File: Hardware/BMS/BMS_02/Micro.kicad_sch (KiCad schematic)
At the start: 21 parts, among them U1 PIC33EP256MC506, U17 CD4051B, U26 CD4051B, U5 CD4051B, Y1 8MHz

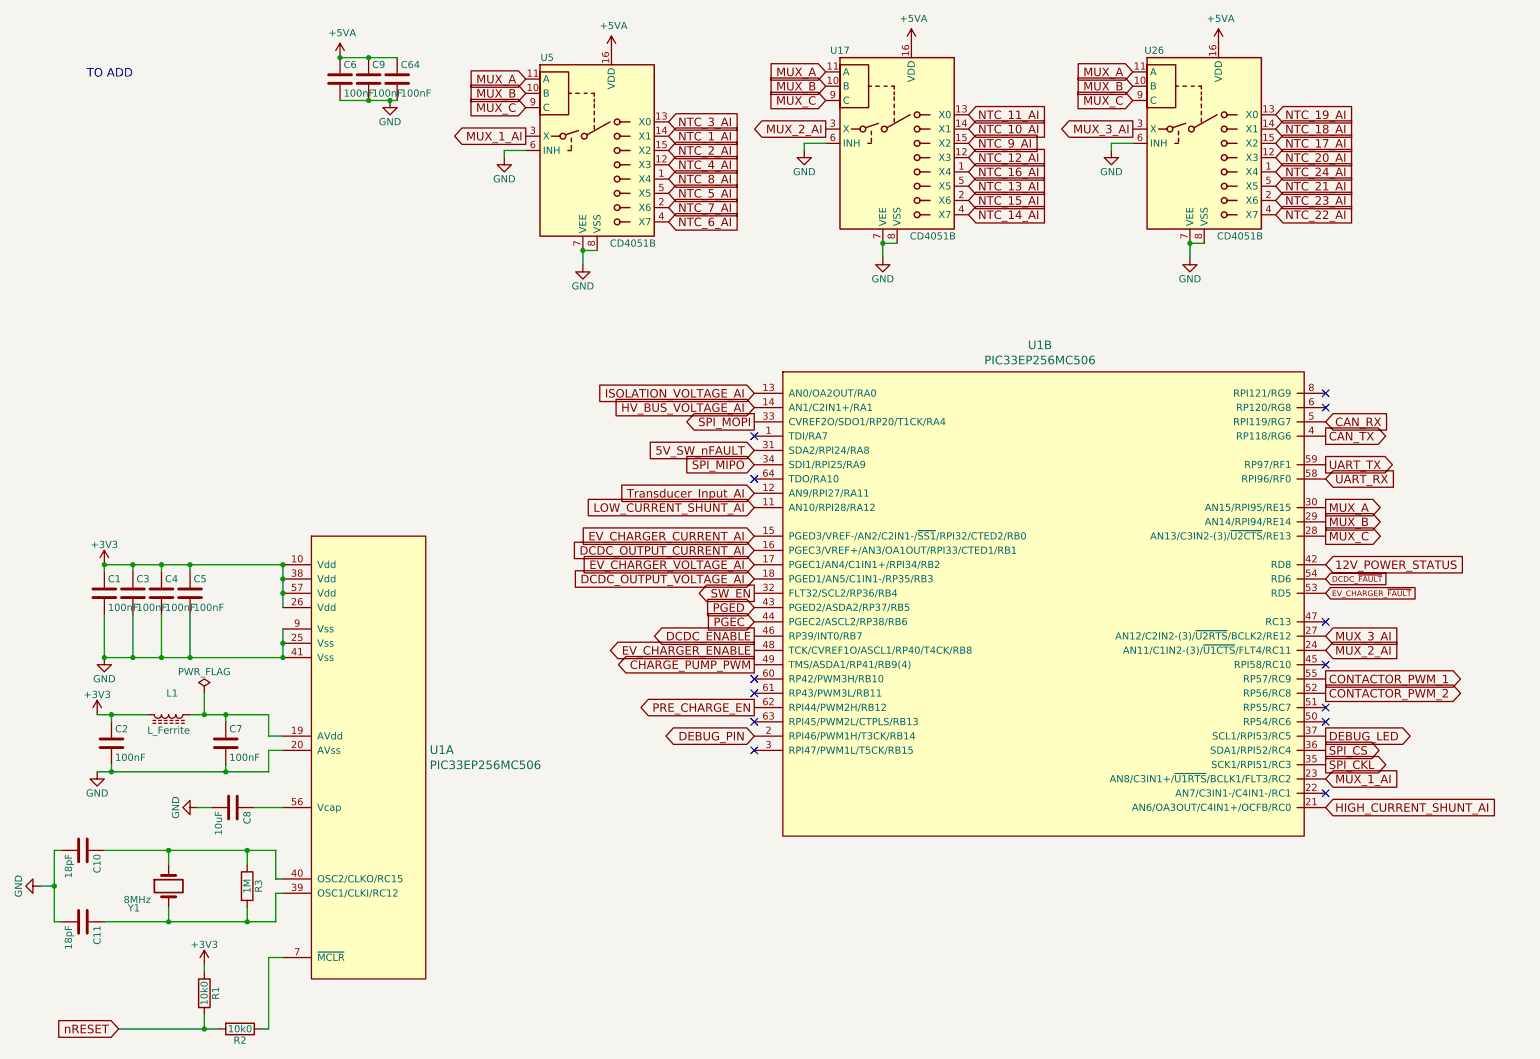
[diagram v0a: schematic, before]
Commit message: bms 02 build and code bring up. Board is built, bootloader is stable and uploads app flawlessly.
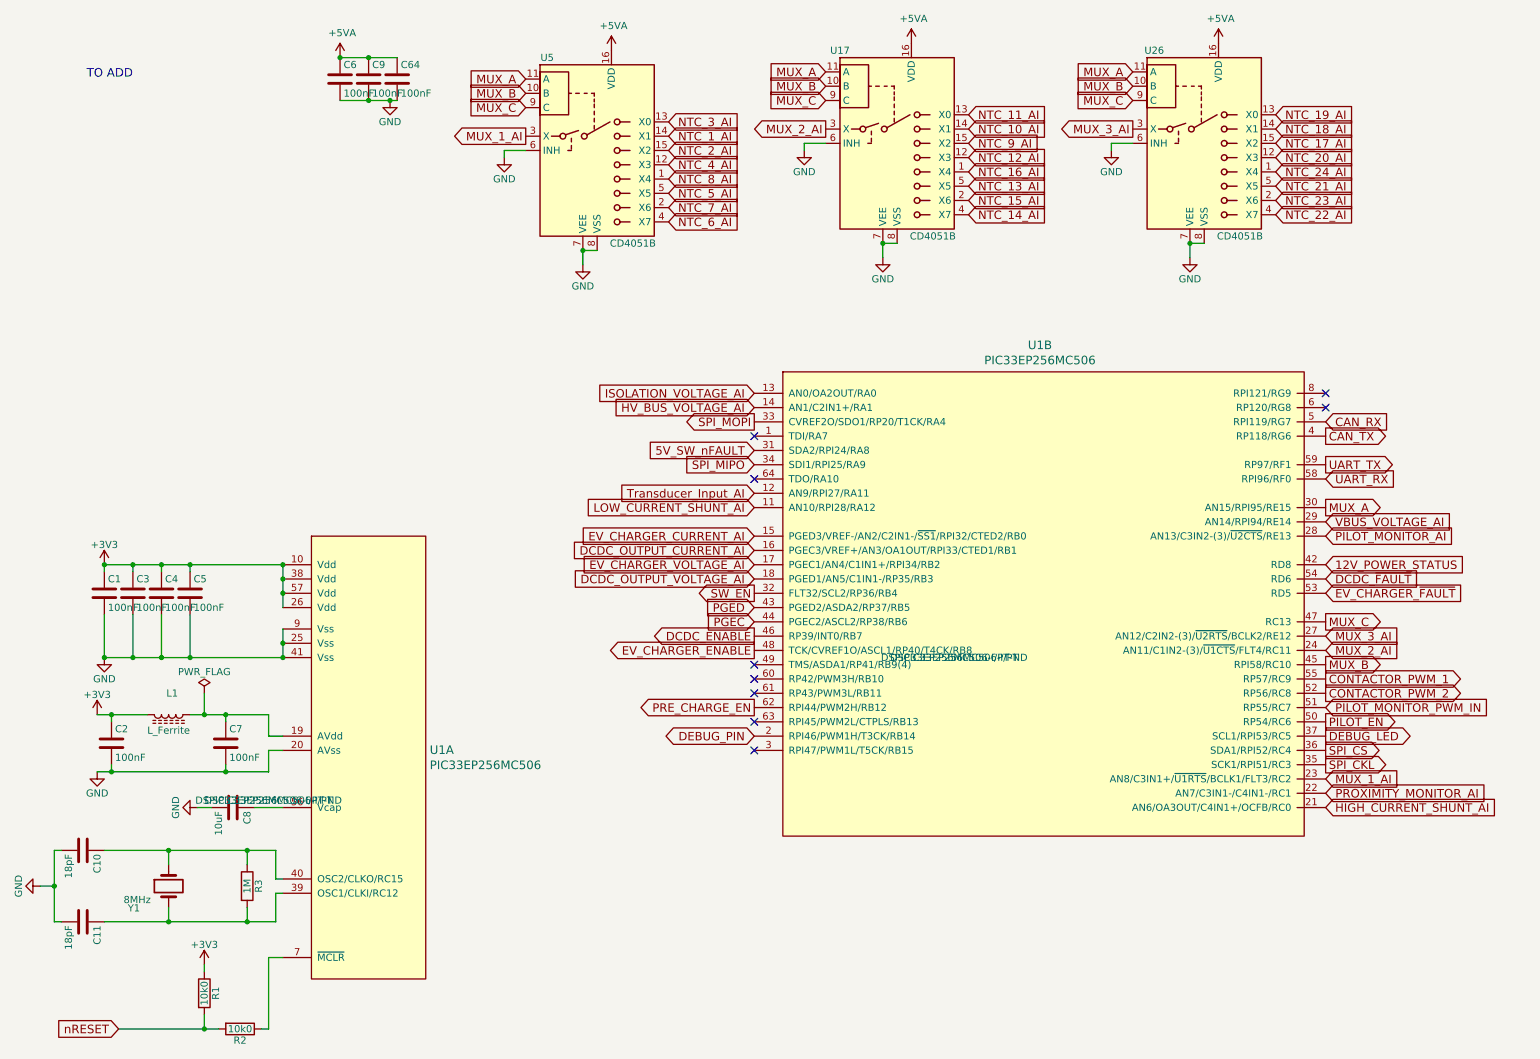
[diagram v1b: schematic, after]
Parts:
- C1, C10, C11, C2, C3, C4, C5, C6, C64, C7, C8, C9, L1, R1, R2, R3: DNP (none) -> (none)
- U1: Digikey_PN (none) -> DSPIC33EP256MC506-I/PT-ND; MPN (none) -> DSPIC33EP256MC506-I/PT
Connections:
- net MUX_B: now also U1.45 (RPI58/RC10); no longer U1.29 (AN14/RPI94/RE14)
- net MUX_C: now also U1.47 (RC13); no longer U1.28 (AN13/C3IN2-(3)/~{U2CTS}/RE13)
- net PROXIMITY_MONITOR_AI: now reaches U1.22 (AN7/C3IN1-/C4IN1-/RC1)
- net PILOT_EN: now reaches U1.50 (RP54/RC6)
- net PILOT_MONITOR_PWM_IN: now reaches U1.51 (RP55/RC7)
- net CHARGE_PUMP_PWM: no longer names the net of U1.49 (TMS/ASDA1/RP41/RB9(4))
- new net PILOT_MONITOR_AI: U1.28 (AN13/C3IN2-(3)/~{U2CTS}/RE13)
- new net VBUS_VOLTAGE_AI: U1.29 (AN14/RPI94/RE14)
- no-connect marks 13 -> 9
